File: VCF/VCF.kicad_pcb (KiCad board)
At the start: 2 copper layers, 33 parts, among them J1 Env, J2 Power, J3 Output, J4 Input, U1 LM324A

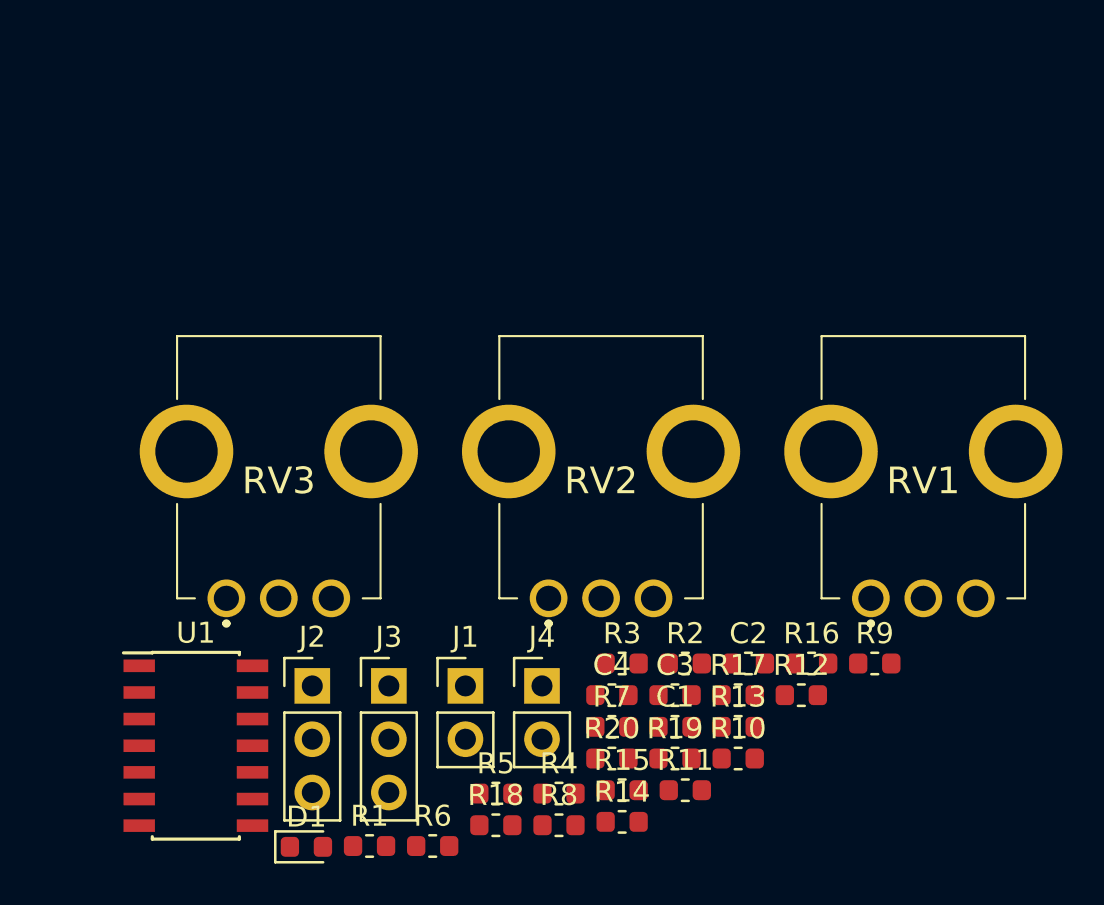
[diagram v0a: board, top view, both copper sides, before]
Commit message: Изменены библиотеки. Добавлинны библиотеки примененные в проекте локально. Добавленны заготовки для печатных плат. Добавленны 3D модели компоненток.
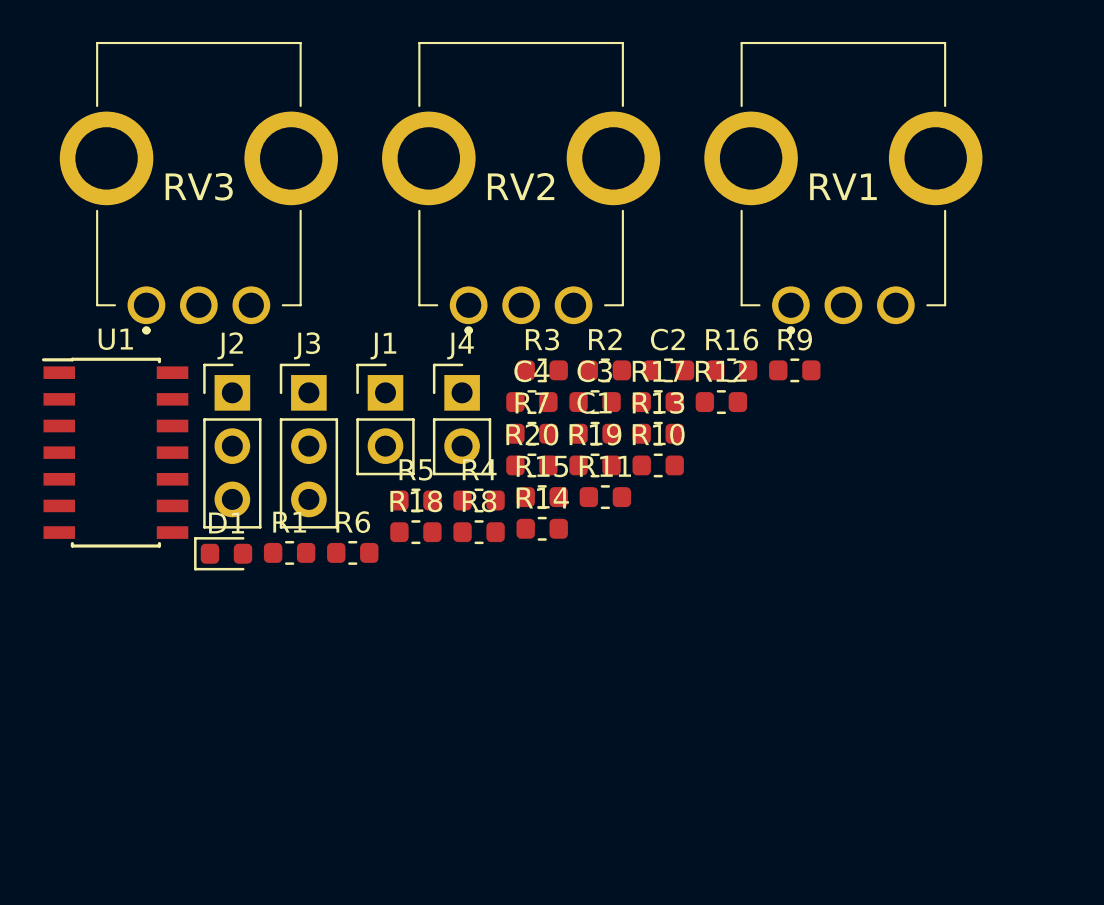
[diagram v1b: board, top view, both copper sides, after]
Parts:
- C1, C2, C3, C4: footprint Capacitor_SMD:C_0603_1608Metric -> footprint:c0603
- D1: footprint Diode_SMD:D_0603_1608Metric -> footprint:d0603
- J1, J4: footprint Connector_PinHeader_2.54mm:PinHeader_1x02_P2.54mm_Vertical -> footprint:pls1x02
- J2, J3: footprint Connector_PinHeader_2.54mm:PinHeader_1x03_P2.54mm_Vertical -> footprint:pls1x03
- R1, R10, R11, R12, R13, R14, R15, R16, R17, R18, R19, R2, R20, R3, R4, R5, R6, R7, R8, R9: footprint Resistor_SMD:R_0603_1608Metric -> footprint:r0603
- RV1, RV2, RV3: footprint R0409N:PTV09A4020FB103 -> footprint:PTV09A4020FB103
- U1: footprint Package_SO:SOIC-14_3.9x8.7mm_P1.27mm -> footprint:soic-14
- moved C3 14.5 mm to (145.9, 80.4)
- moved C4 14.5 mm to (142.9, 80.4)
- moved R12 14.5 mm to (152.0, 80.4)
- moved R17 14.5 mm to (149.0, 80.4)
- moved C1 14.5 mm to (145.9, 81.9)
- moved C2 14.5 mm to (149.4, 78.9)
- moved D1 14.5 mm to (128.4, 87.6)
- moved J1 14.5 mm to (136.0, 80.0)
- moved J2 14.5 mm to (128.7, 80.0)
- moved J3 14.5 mm to (132.3, 80.0)
- moved J4 14.5 mm to (139.6, 80.0)
- moved R1 14.5 mm to (131.4, 87.6)
- moved R10 14.5 mm to (149.0, 83.4)
- moved R11 14.5 mm to (146.4, 84.9)
- moved R13 14.5 mm to (149.0, 81.9)
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
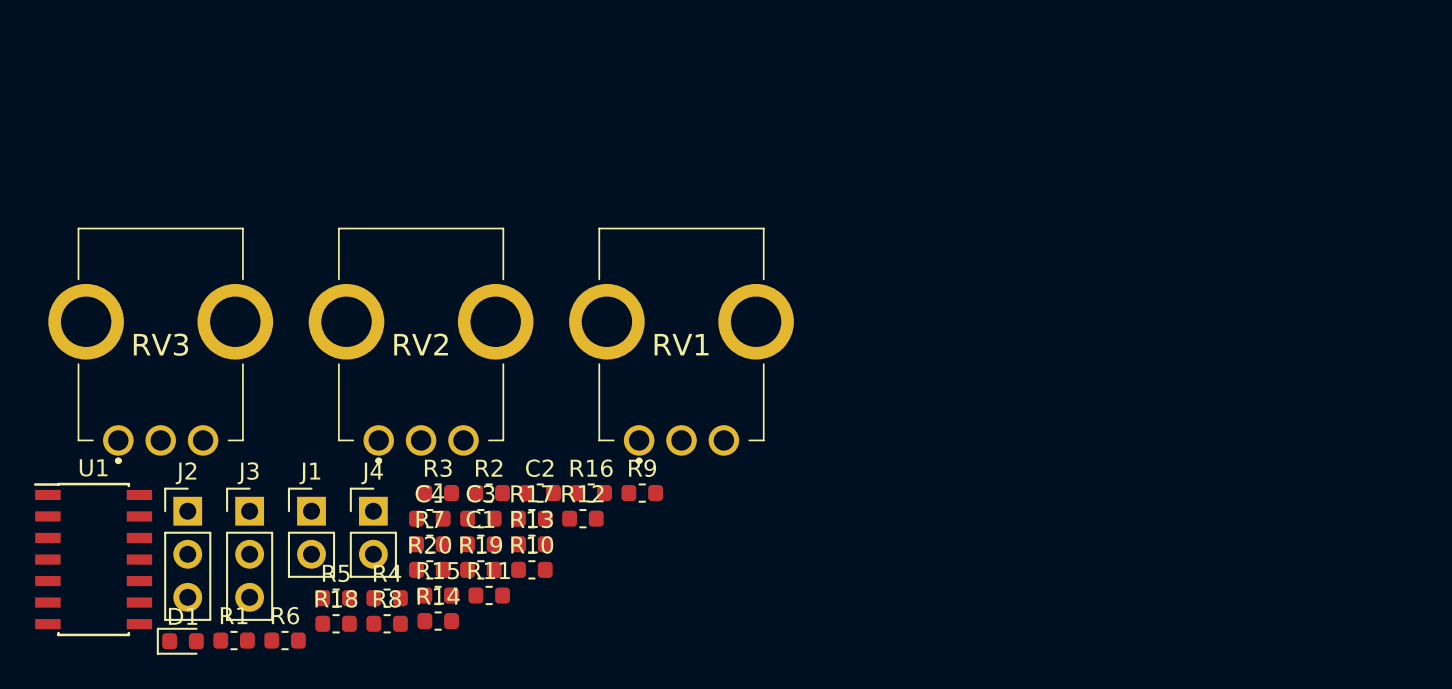
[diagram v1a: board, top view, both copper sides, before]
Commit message: Исправленну ошибки в схемах. Полностью локальные библиотеки и 3D модели.
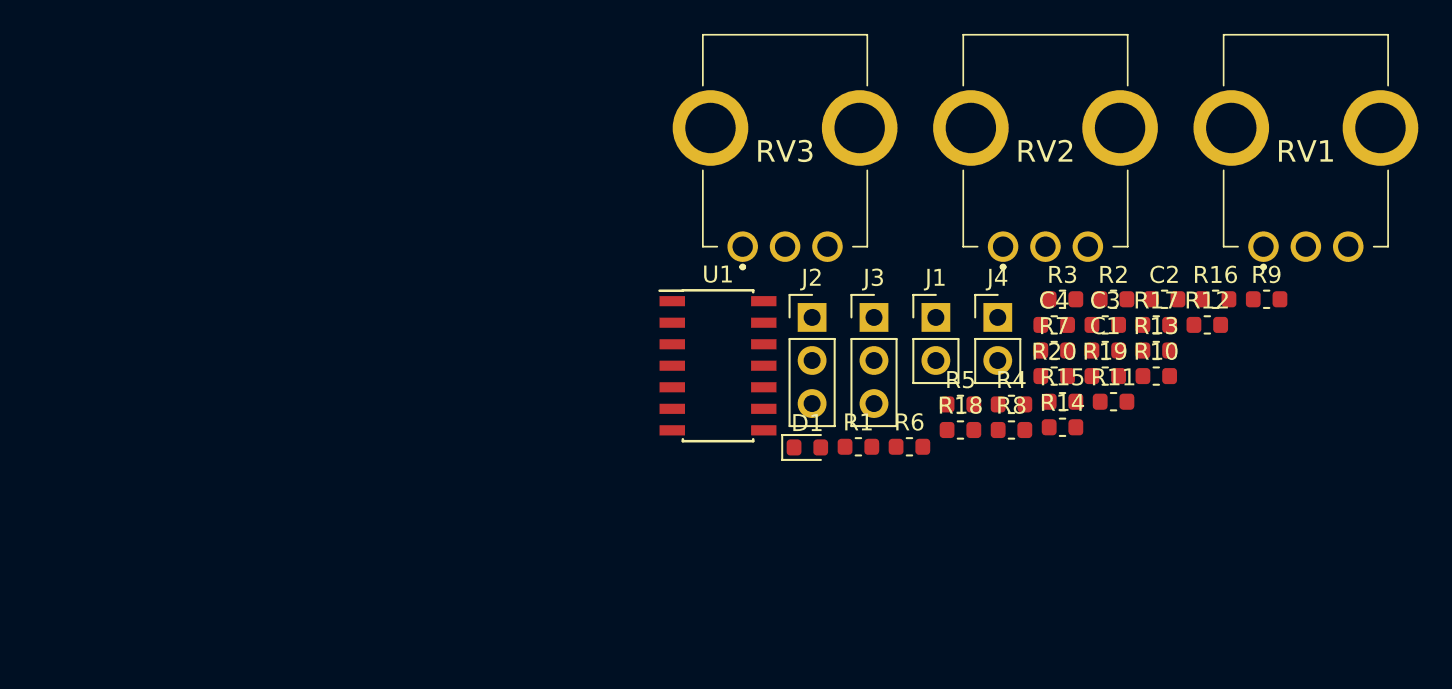
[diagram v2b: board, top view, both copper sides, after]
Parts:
- moved C2 38.6 mm to (186.3, 67.5)
- moved R1 38.6 mm to (168.2, 76.2)
- moved R19 38.6 mm to (182.8, 72.0)
- moved R2 38.6 mm to (183.3, 67.5)
- moved R20 38.6 mm to (179.8, 72.0)
- moved R4 38.6 mm to (177.2, 73.7)
- moved R5 38.6 mm to (174.2, 73.7)
- moved R9 38.6 mm to (192.3, 67.5)
- moved RV1 38.6 mm to (194.6, 58.8)
- moved RV3 38.6 mm to (163.9, 58.8)
- moved C1 38.6 mm to (182.8, 70.5)
- moved C3 38.6 mm to (182.8, 69.0)
- moved C4 38.6 mm to (179.8, 69.0)
- moved D1 38.6 mm to (165.2, 76.2)
- moved J2 38.6 mm to (165.5, 68.5)
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
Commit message: Изменение в схемах. Разведенны ПП
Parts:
- added J10: Conn_01x05_Male, footprint:pls1x05, B.Cu at (48.3, 24.0)
- added J11: Input, footprint:pls1x02, F.Cu at (26.7, 66.0)
- added J12: Conn_01x05_Male, footprint:pls1x05, B.Cu at (25.4, 24.0)
- added J5: Conn_01x05_Male, footprint:pls1x05, B.Cu at (72.4, 78.0)
- added J6: Conn_01x05_Male, footprint:pls1x05, B.Cu at (24.1, 78.0)
- added J7: Conn_01x05_Male, footprint:pls1x05, B.Cu at (47.0, 78.0)
- added J8: Conn_01x05_Male, footprint:pls1x05, B.Cu at (73.7, 24.0)
- added J9: Output, footprint:pls1x03, F.Cu at (81.3, 57.1)
- C1, C2, C3, C4, D1, R1, R10, R11, R12, R13, R14, R15, R16, R17, R18, R19, R2, R20, R3, R4, R5, R6, R7, R8, R9, U1: moved to B.Cu
- J1: value Env -> Conn_01x05_Male; footprint footprint:pls1x02 -> footprint:pls1x05; moved to B.Cu
- J2: value Power -> Conn_01x05_Male; footprint footprint:pls1x03 -> footprint:pls1x05; moved to B.Cu
- J3: value Output -> Env; footprint footprint:pls1x03 -> footprint:pls1x02
- J4: value Input -> Conn_01x05_Male; footprint footprint:pls1x02 -> footprint:pls1x05; moved to B.Cu
- RV1, RV2, RV3: footprint footprint:PTV09A4020FB103 -> footprint:R0904N
- moved RV1 160.9 mm to (34.9, 39.5)
- moved R16 158.3 mm to (31.0, 64.1), turned to 180 degrees
- moved J4 151.9 mm to (25.4, 85.0), turned to 270 degrees
- moved R19 151.9 mm to (31.0, 66.0)
- moved R3 149.9 mm to (30.8, 55.8), turned to 180 degrees
- moved R20 148.8 mm to (31.0, 68.6)
- moved R9 143.6 mm to (49.5, 52.5), turned to 90 degrees
- moved R18 143.4 mm to (30.9, 71.0), turned to 180 degrees
- moved J3 143.0 mm to (26.7, 55.9)
- moved R7 133.8 mm to (46.0, 67.3), turned to 270 degrees
- moved R8 133.6 mm to (43.9, 67.3), turned to 270 degrees
- moved C2 133.5 mm to (52.8, 68.2)
- moved C3 132.4 mm to (50.4, 69.0), turned to 90 degrees
- moved C1 130.9 mm to (52.6, 56.8)
- moved R10 128.6 mm to (57.1, 73.7), turned to 270 degrees
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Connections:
- J1 pad 1: /ENV_2 -> +5V
- J1 pad 2: /ENV_2 -> +5V
- J2 pad 2: GNDREF -> +5V
- J2 pad 3: -5V -> +5V
- J3 pad 1: /OUT_1 -> /ENV_2
- J3 pad 2: /OUT_2 -> /ENV_2
- J4 pad 1: Net-(J4-Pad1) -> +5V
- J4 pad 2: /IN_2 -> +5V
- R16 pad 2: Net-(J4-Pad1) -> Net-(J11-Pad1)
- R17 pad 1: Net-(J3-Pad3) -> Net-(J9-Pad3)
- R19 pad 1: Net-(J4-Pad1) -> Net-(J11-Pad1)
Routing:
- net GNDREF: track 0.00 -> 218.7 mm, vias 0 -> 6
- net -5V: track 0.00 -> 199.6 mm, vias 0 -> 1
- net +5V: track 0.00 -> 152.3 mm, vias 0 -> 2
- net Net-(R16-Pad1): track 0.00 -> 71.3 mm, vias 0 -> 2
- net Net-(R12-Pad2): track 0.00 -> 49.8 mm, vias 0 -> 2
- net Net-(C3-Pad1): track 0.00 -> 35.5 mm, vias 0 -> 2
- net Net-(RV1-Pad2): track 0.00 -> 33.1 mm
- net /ENV_2: track 0.00 -> 29.9 mm
- net Net-(R3-Pad1): track 0.00 -> 29.2 mm
- net Net-(C3-Pad2): track 0.00 -> 28.4 mm
- net Net-(R6-Pad2): track 0.00 -> 26.2 mm
- net Net-(C4-Pad1): track 0.00 -> 16.7 mm
- net Net-(R6-Pad1): track 0.00 -> 16.0 mm, vias 0 -> 2
- net Net-(R9-Pad2): track 0.00 -> 15.7 mm
- net Net-(R10-Pad1): track 0.00 -> 9.96 mm
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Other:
- board outline added: 70 x 70 mm
- net class power added: clearance 0.2, trace_width 0.5, via_dia 0.8, via_drill 0.4
